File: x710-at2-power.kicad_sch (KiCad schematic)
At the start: 6 parts, among them U4 EZX710AT2_S_LMR5

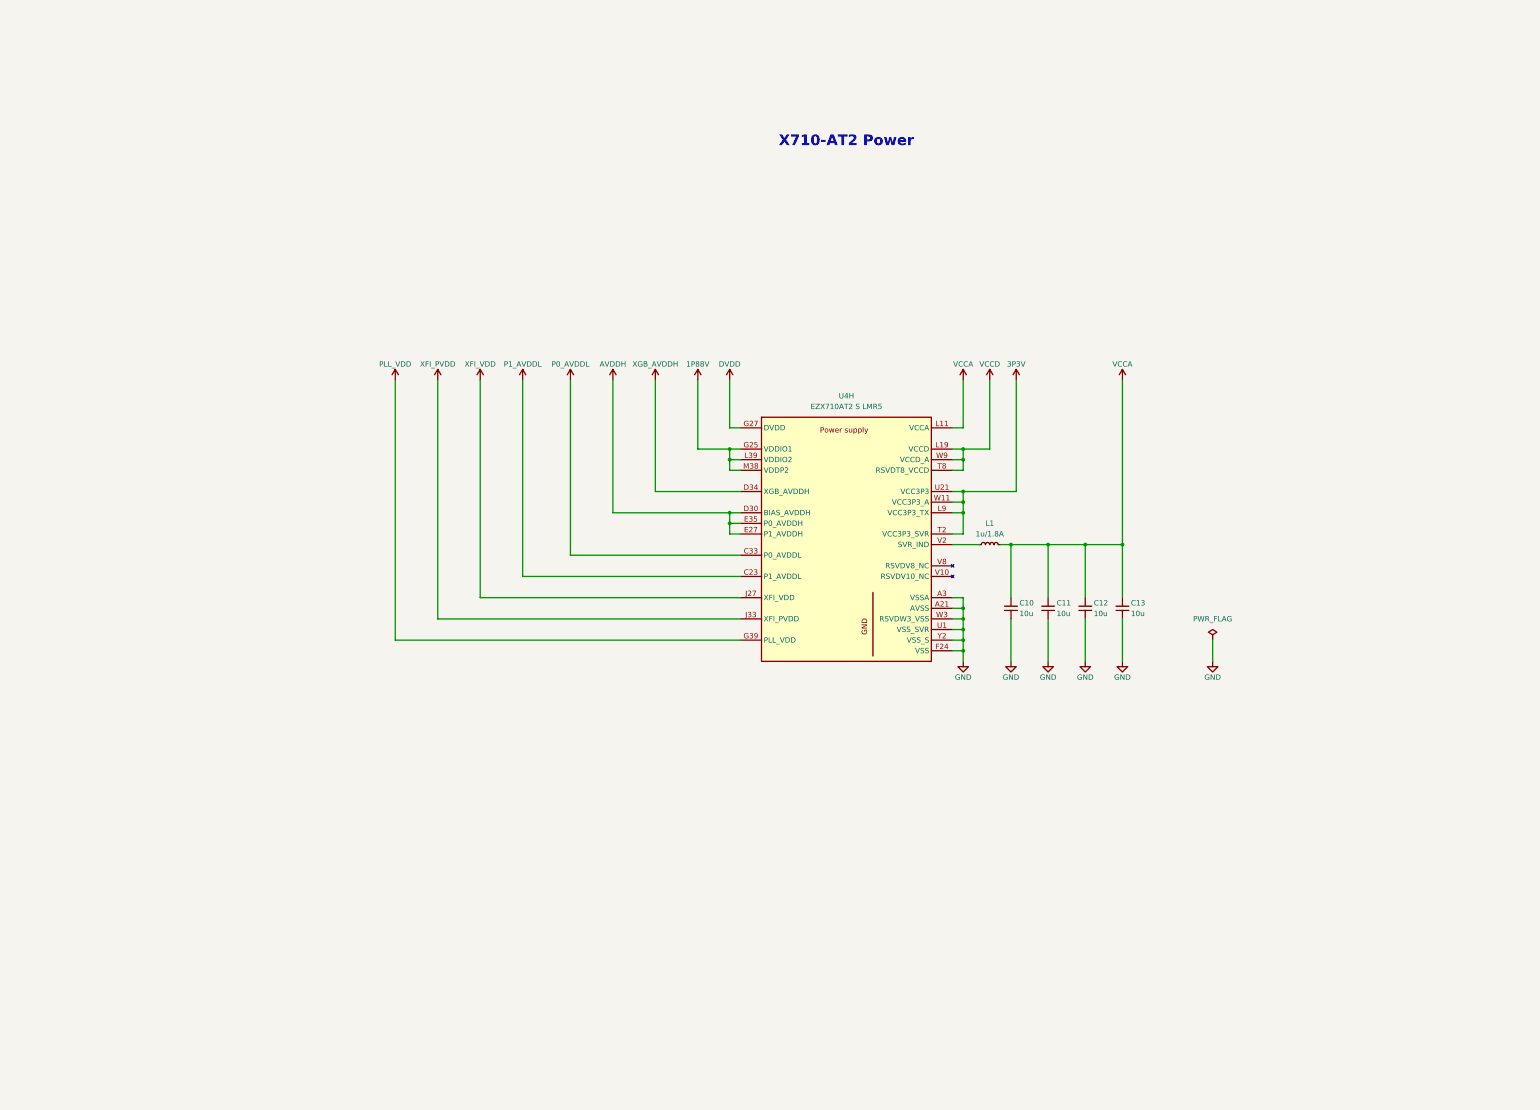
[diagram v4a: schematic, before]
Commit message: [#80813] WIP: Add decoupling capacitors
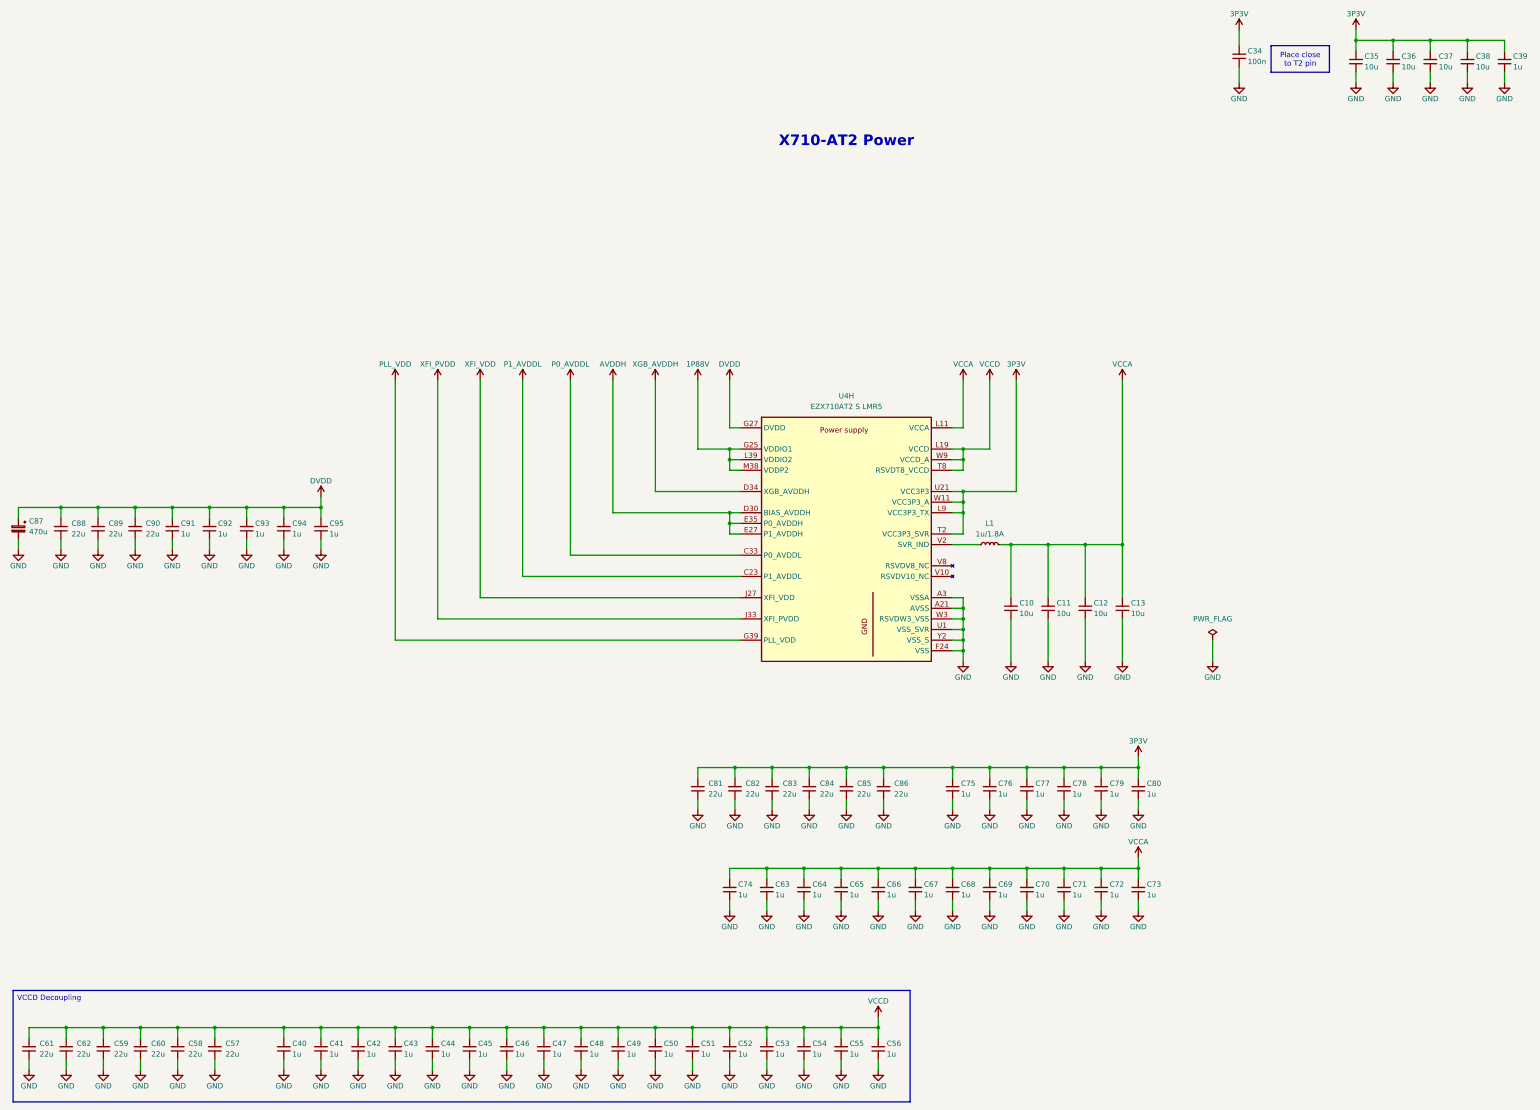
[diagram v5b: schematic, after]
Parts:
- added C34: C_100n_16V_X7R_0402, antmicro-footprints:C_0402_1005Metric, symbol antmicroCapacitors0402:C_100n_16V_X7R_0402
- added C35, C36, C37, C38: C_10u_10V_X7R_0603, antmicro-footprints:C_0603_1608Metric, symbol antmicroCapacitors0603:C_10u_10V_X7R_0603
- added C39, C40, C41, C42, C43, C44, C45, C46, C47, C48, C49, C50, C51, C52, C53, C54, C55, C56, C63, C64, C65, C66, C67, C68, C69, C70, C71, C72, C73, C74, C75, C76, C77, C78, C79, C80, C91, C92, C93, C94, C95: C_1u_25V_0402, antmicro-footprints:C_0402_1005Metric, symbol antmicroCapacitors0402:C_1u_25V_0402
- added C57, C58, C59, C60, C61, C62, C81, C82, C83, C84, C85, C86, C88, C89, C90: C_22u_16V_0603, antmicro-footprints:C_0603_1608Metric_EIA, symbol antmicroCapacitors0603:C_22u_16V_0603
- added C87: C_Pol_470u_6.3V_Vishay-TR3-D, antmicro-footprints:C_Pol_EIA-D, symbol antmicroCapacitorspol:C_Pol_470u_6.3V_Vishay-TR3-D
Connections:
- net 3P3V: now also C34.2, C35.2, C36.2, C37.2, C38.2, C39.2, C75.2, C76.2, C77.2, C78.2, C79.2, C80.2, C81.2, C82.2, C83.2, C84.2, C85.2, C86.2
- net DVDD: now also C87.1, C88.2, C89.2, C90.2, C91.2, C92.2, C93.2, C94.2, C95.2
- net GND: now also C34.1, C35.1, C36.1, C37.1, C38.1, C39.1, C40.1, C41.1, C42.1, C43.1, C44.1, C45.1, C46.1, C47.1, C48.1, C49.1, C50.1, C51.1, C52.1, C53.1, C54.1, C55.1, C56.1, C57.1, C58.1, C59.1, C60.1, C61.1, C62.1, C63.1, C64.1, C65.1, C66.1, C67.1, C68.1, C69.1, C70.1, C71.1, C72.1, C73.1, C74.1, C75.1, C76.1, C77.1, C78.1, C79.1, C80.1, C81.1, C82.1, C83.1, C84.1, C85.1, C86.1, C87.2, C88.1, C89.1, C90.1, C91.1, C92.1, C93.1, C94.1, C95.1
- net VCCA: now also C63.2, C64.2, C65.2, C66.2, C67.2, C68.2, C69.2, C70.2, C71.2, C72.2, C73.2, C74.2
- net VCCD: now also C40.2, C41.2, C42.2, C43.2, C44.2, C45.2, C46.2, C47.2, C48.2, C49.2, C50.2, C51.2, C52.2, C53.2, C54.2, C55.2, C56.2, C57.2, C58.2, C59.2, C60.2, C61.2, C62.2

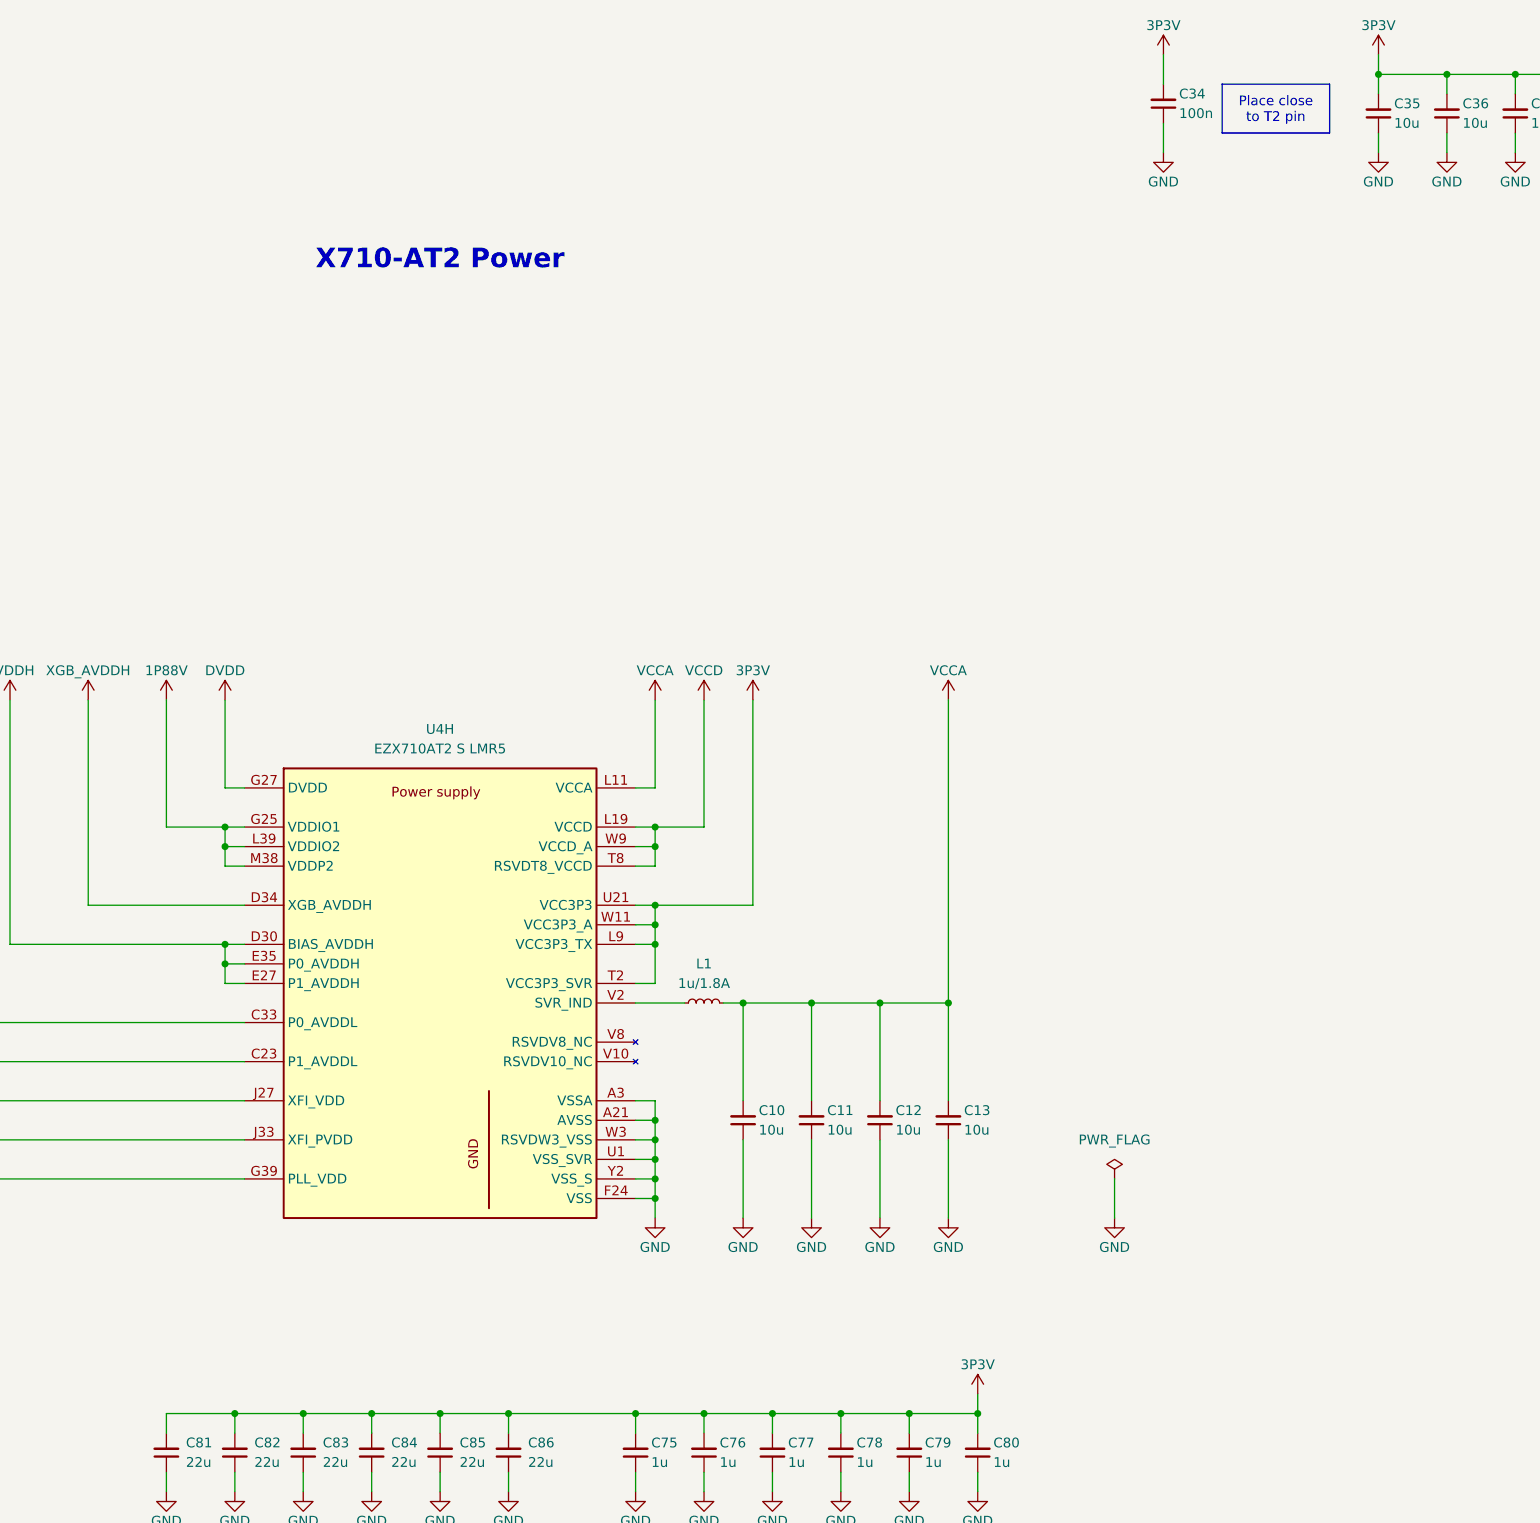
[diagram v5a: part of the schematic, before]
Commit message: [#80813] Change 3V3 and 1V88 power rails names
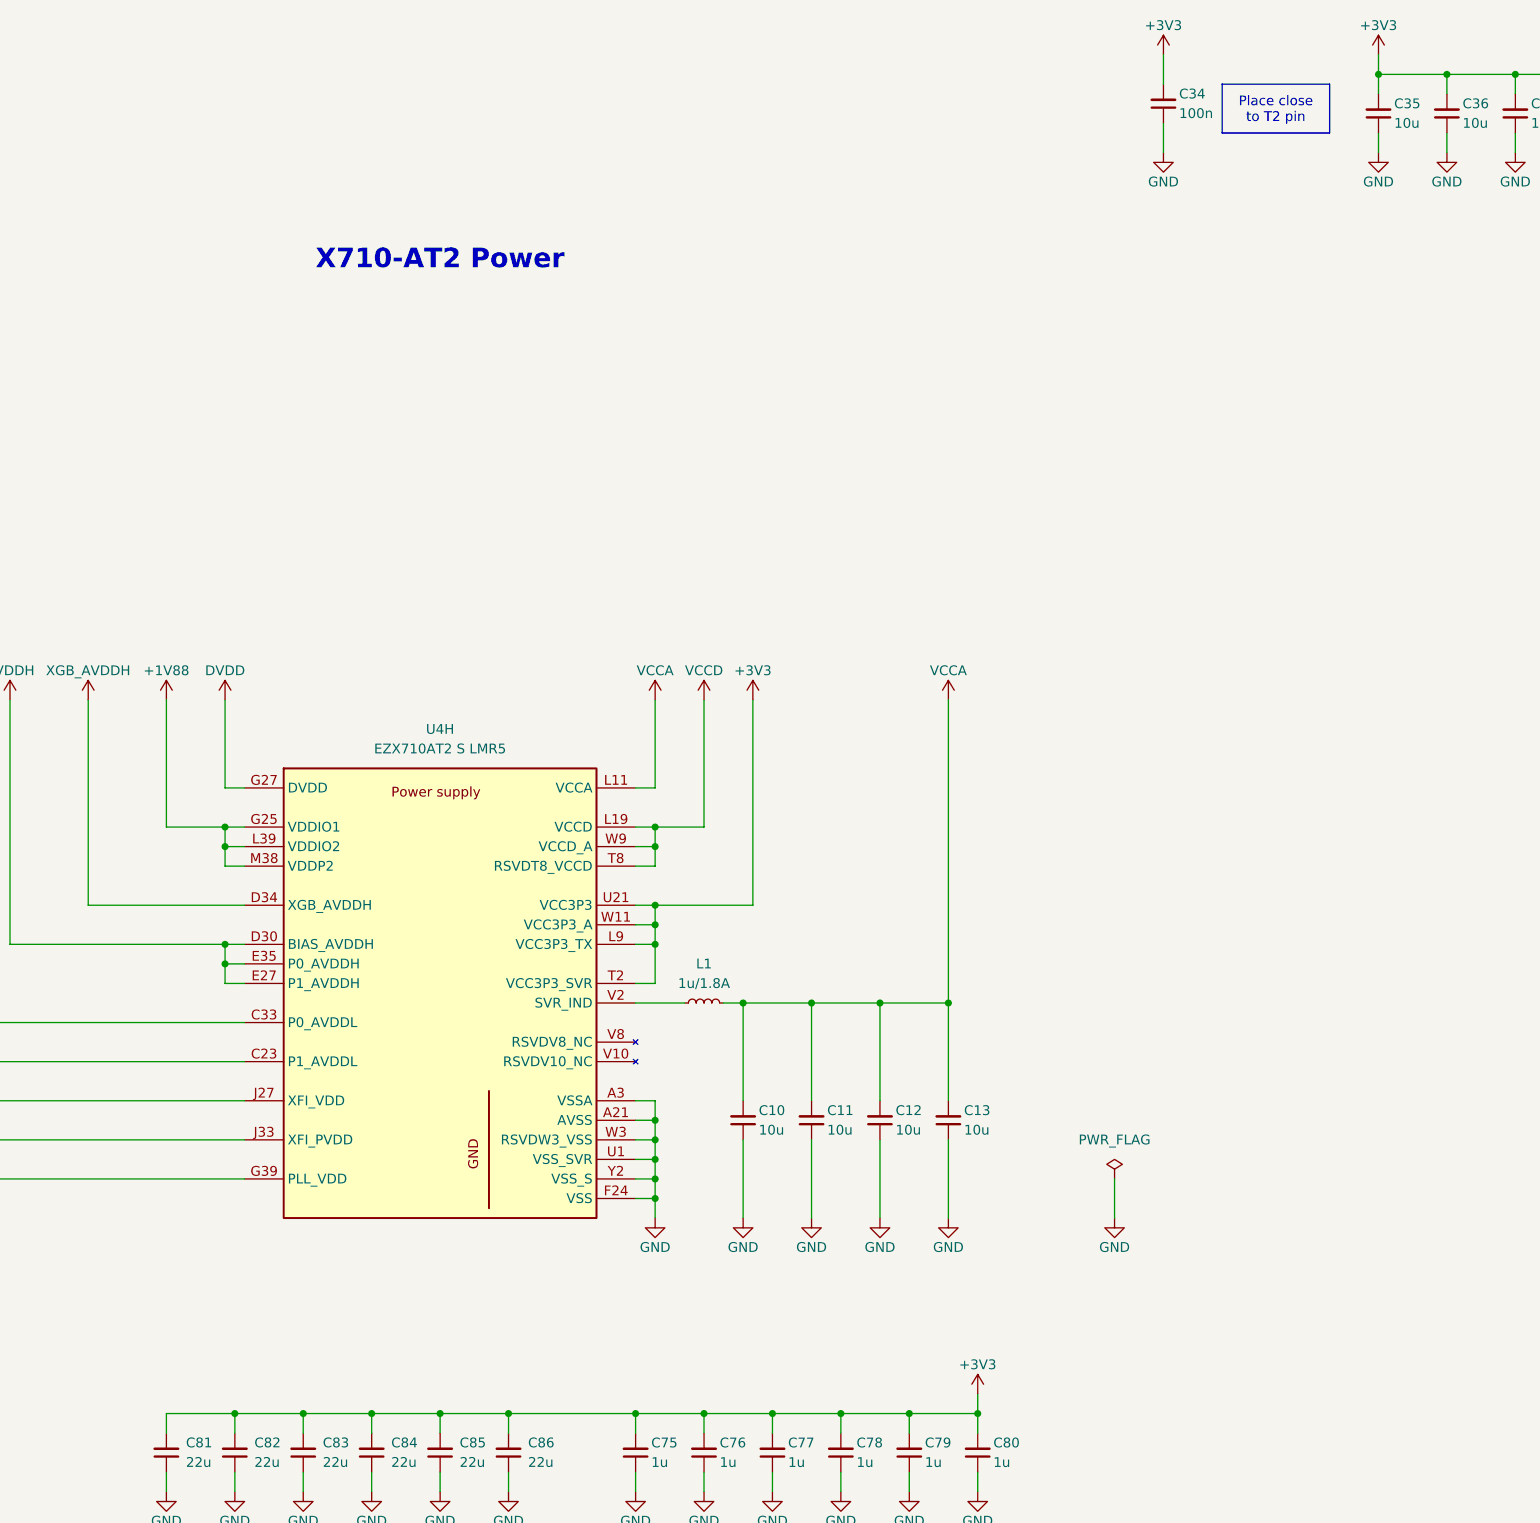
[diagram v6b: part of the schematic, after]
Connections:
- net 1P88V renamed +1V88
- net 3P3V renamed +3V3

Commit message: [#80813] Adjust passives values, add remaining decoupling capacitors
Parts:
- removed L1: L_1u_1.8A_0603, antmicro-footprints:L_0603_1608Metric, symbol antmicroFixedInductors:L_1u_1.8A_0603
- added C108: C_Pol_470u_6.3V_Vishay-TR3-D, antmicro-footprints:C_Pol_EIA-D, symbol antmicroCapacitorspol:C_Pol_470u_6.3V_Vishay-TR3-D
- added C109, C111: C_22u_16V_0603, antmicro-footprints:C_0603_1608Metric_EIA, symbol antmicroCapacitors0603:C_22u_16V_0603
- added C110, C112, C127, C135, C141, C144, C152: C_100n_16V_X7R_0402, antmicro-footprints:C_0402_1005Metric, symbol antmicroCapacitors0402:C_100n_16V_X7R_0402
- added C113, C114, C115, C116, C120, C121, C122, C123, C128, C129, C130, C131, C134, C136, C137, C138, C139, C142, C145, C148, C149, C150, C151, C153: C_1u_25V_0402, antmicro-footprints:C_0402_1005Metric, symbol antmicroCapacitors0402:C_1u_25V_0402
- added C117, C124, C132, C133, C143, C146, C147: C_10u_10V_X7R_0603, antmicro-footprints:C_0603_1608Metric, symbol antmicroCapacitors0603:C_10u_10V_X7R_0603
- added C118, C119, C125, C126: C_100u_0805, antmicro-footprints:C_0805_2012Metric, symbol antmicroCapacitorsmisc:C_100u_0805
- added C140: C_47u_50V_X7R_0402, antmicro-footprints:C_0402_1005Metric, symbol antmicroCapacitors0402:C_47u_50V_X7R_0402
- added FB2, FB4, FB5: FB_33Z_3A_Murata-BLM18PG_0603, antmicro-footprints:FB_0603_1608Metric, symbol antmicroFerriteBeadsandChips:FB_33Z_3A_Murata-BLM18PG_0603
- added FB6, FB7: FB_470Z_1A_Murata-BLM18PG_0603, antmicro-footprints:FB_0603_1608Metric, symbol antmicroFerriteBeadsandChips:FB_470Z_1A_Murata-BLM18PG_0603
- added L4, L5: L_4u7_0.4A_0805, antmicro-footprints:L_0805_2012Metric, symbol antmicroFixedInductors:L_4u7_0.4A_0805
- added L6: L_1u_11A_Coilcraft-XFL4020, antmicro-footprints:L_Coilcraft-XFL4020, symbol antmicroFixedInductors:L_1u_11A_Coilcraft-XFL4020
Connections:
- net +1V88: now also C127.2, C146.2, C147.2, C148.2, C149.2, C150.2, C151.2, C152.2, FB5.1, FB7.1
- net AVDDH: now also C128.2, C129.2, C130.2, C131.2, C132.2, C133.2, C134.2, FB5.2
- net GND: now also C108.2, C109.1, C110.1, C111.1, C112.1, C113.1, C114.1, C115.1, C116.1, C117.1, C118.1, C119.1, C120.1, C121.1, C122.1, C123.1, C124.1, C125.1, C126.1, C127.1, C128.1, C129.1, C130.1, C131.1, C132.1, C133.1, C134.1, C135.1, C136.1, C137.1, C138.1, C139.1, C140.1, C141.1, C142.1, C143.1, C144.1, C145.1, C146.1, C147.1, C148.1, C149.1, C150.1, C151.1, C152.1, C153.1
- net P0_AVDDL: now also C113.2, C114.2, C115.2, C116.2, C117.2, C118.2, C119.2, FB2.2
- net P1_AVDDL: now also C120.2, C121.2, C122.2, C123.2, C124.2, C125.2, C126.2, FB4.2
- net PLL_VDD: now also C145.2, FB6.2
- net VCCA: now also L6.2
- net XFI_PVDD: now also C142.2, C143.2, L5.2
- net XFI_VDD: now also C136.2, C137.2, C138.2, C139.2, C140.2, L4.2
- net XGB_AVDDH: now also C153.2, FB7.2
- net at U4.V2 (SVR_IND): now also L6.1
- new net +1V0: C108.1, C109.2, C110.2, C111.2, C112.2, C135.2, C141.2, C144.2, FB2.1, FB4.1, FB6.1, L4.1, L5.1
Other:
- moved on the sheet: C10, C11, C12, C13, C34, C35, C36, C37, C38, C39, C40, C41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
